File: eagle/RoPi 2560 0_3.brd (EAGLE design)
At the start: 85.1 x 56.1 mm, 51 parts, among them J1 AVR_SPI_PRG_6PTH, U1 ATMEGA2560AU, U2 MAX3378EEUD, U3 L298_BRIDGE_DRIVER, U4 L298_BRIDGE_DRIVER, Y1 16M

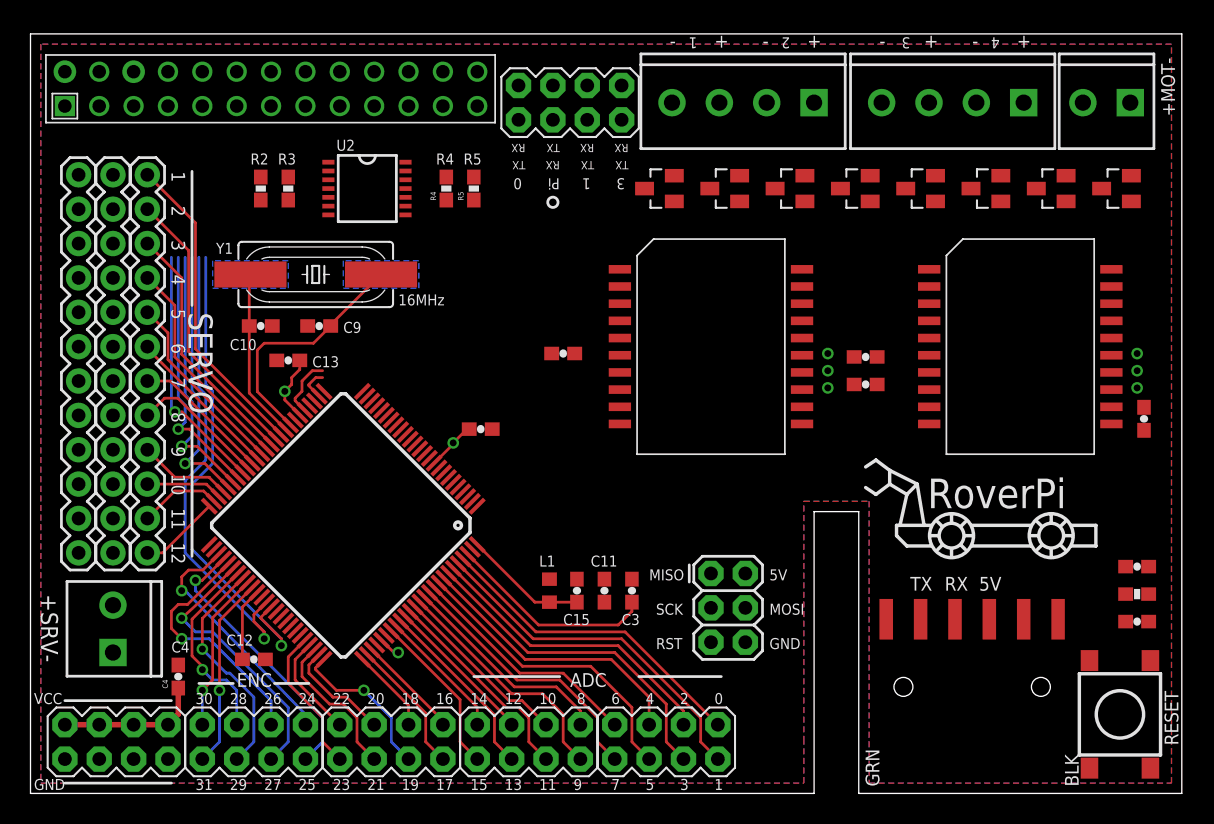
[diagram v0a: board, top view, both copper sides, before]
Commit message: Updated name to RoverPi, moved arduino library into /arduino/RoverPi
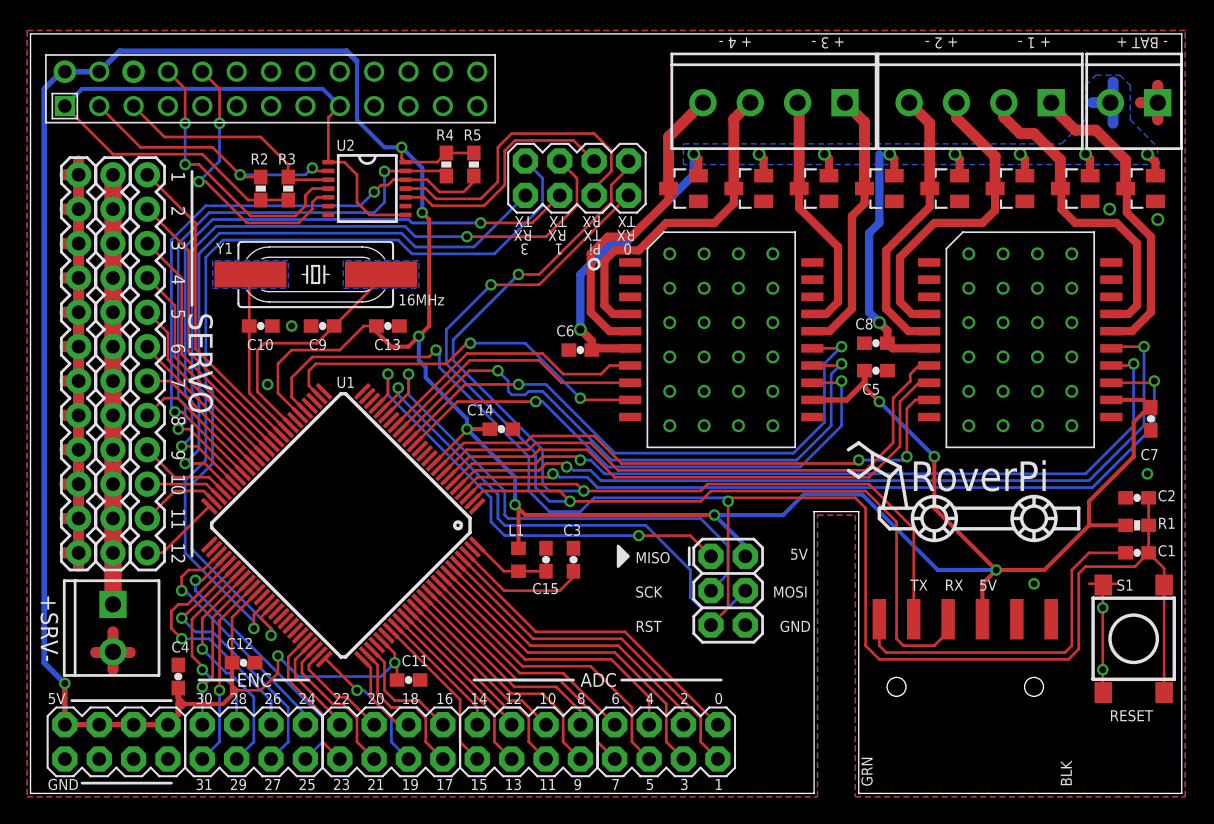
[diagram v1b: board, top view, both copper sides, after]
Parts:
- moved C11 15.9 mm to (27.9, 8.38), turned to 0 degrees
- moved C2 9.14 mm to (81.8, 21.8)
- moved C13 7.79 mm to (26.4, 34.5), turned to 0 degrees
- moved S1 5.68 mm to (81.5, 11.4)
- moved U$1 5.61 mm to (40.4, 45.5), turned to 180 degrees
- moved R1 5.08 mm to (81.8, 19.8)
- moved C3 4.89 mm to (40.1, 17.3)
- moved JP3 3.56 mm to (6.10, 14.0), turned to 270 degrees
- moved C15 3.23 mm to (38.1, 17.3)
- moved L1 3.23 mm to (36.1, 17.3)
- moved JP4 2.29 mm to (60.2, 51.1)
- moved JP2 2.03 mm to (83.3, 51.1)
- moved JP5 2.03 mm to (75.4, 51.1)
- moved D5 1.78 mm to (72.4, 44.7)
- moved D7 1.78 mm to (82.0, 44.7)
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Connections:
- net GND: now also JP3.2; no longer JP3.1
- net MOT1+: now also D7.3, JP5.1, U4.16; no longer D1.3, JP4.2, U3.4
- net MOT1-: now also D8.3, JP5.2, U4.17; no longer D2.3, JP4.1, U3.5
- net MOT1_A: now also U1.4, U4.13; no longer U1.18, U3.7
- net MOT1_B: now also U1.5, U4.15; no longer U1.27, U3.9
- net MOT1_PWM: now also U1.6, U4.14; no longer U1.17, U3.8
- net MOT2+: now also D5.3, JP5.3, U4.4; no longer D3.3, JP4.4, U3.16
- net MOT2-: now also D6.3, JP5.4, U4.5; no longer D4.3, JP4.3, U3.17
- net MOT2_A: now also U1.8, U4.7; no longer U1.14, U3.13
- net MOT2_B: now also U1.9, U4.9; no longer U1.15, U3.15
- net MOT2_PWM: now also U1.7, U4.8; no longer U1.16, U3.14
- net MOT3+: now also D3.3, JP4.1, U3.16; no longer D5.3, JP5.2, U4.4
- net MOT3-: now also D4.3, JP4.2, U3.17; no longer D6.3, JP5.1, U4.5
- net MOT3_A: now also U1.14, U3.13; no longer U1.8, U4.7
- net MOT3_B: now also U1.15, U3.15; no longer U1.9, U4.9
- net MOT3_PWM: now also U1.16, U3.14; no longer U1.7, U4.8
- net MOT4+: now also D1.3, JP4.3, U3.4; no longer D7.3, JP5.4, U4.16
- net MOT4-: now also D2.3, JP4.4, U3.5; no longer D8.3, JP5.3, U4.17
- net MOT4_A: now also U1.18, U3.7; no longer U1.4, U4.13
- net MOT4_B: now also U1.27, U3.9; no longer U1.5, U4.15
- net MOT4_PWM: now also U1.17, U3.8; no longer U1.6, U4.14
- net N$1: now also JP3.1; no longer JP3.2
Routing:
- net 5V: track 26.6 -> 283.6 mm, vias 3 -> 12
- net GND: track 0.00 -> 112.8 mm, vias 0 -> 56
- net RST: track 4.53 -> 116.6 mm, vias 0 -> 2
- net RX0: track 0.00 -> 82.2 mm, vias 0 -> 2
- net TX0: track 0.00 -> 78.0 mm, vias 0 -> 2
- net N$1: track 0.00 -> 63.5 mm
- net MOT1_A: track 0.00 -> 60.5 mm, vias 0 -> 2
- net MOT1_B: track 2.41 -> 61.9 mm, vias 0 -> 2
- net MOT1_PWM: track 0.00 -> 59.3 mm, vias 0 -> 2
- net V_BATT: track 0.00 -> 58.6 mm, vias 0 -> 10
- net 3.3V: track 0.00 -> 53.8 mm
- net MOT3_PWM: track 0.00 -> 45.0 mm, vias 0 -> 2
- net MOT3_B: track 0.00 -> 43.7 mm, vias 0 -> 2
- net MOT2_A: track 0.00 -> 43.1 mm
- net MOT3_A: track 0.00 -> 42.1 mm, vias 0 -> 2
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- added copper zone on layer 16, net V_BATT
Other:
- board text added: "+ 1 -"
- board text added: "+ 2 -"
- board text added: "+ 3 -"
- board text added: "+ 4 -"
- board text added: "- BAT +"
- board text added: "C1"
- board text added: "C14"
- board text added: "C2"
- board text added: "C5"
- board text added: "C6"
- board text added: "C7"
- board text added: "C8"
- board text added: "Mar 21, 2014"
- board text added: "R1"
- board text added: "Rev 0.3"
- board text added: "S1"
- board text added: "U1"
- board text added: "dbommarito.com/roverpi"
- board text removed: "+"
- board text removed: "+MOT-"
- board text removed: "-"
- board text removed: "VCC"
